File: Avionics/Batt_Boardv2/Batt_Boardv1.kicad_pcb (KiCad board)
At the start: 2 copper layers, 90.2 x 95.9 mm, 30 parts, among them J1 Conn_02x26_Odd_Even, J2 Conn_02x26_Odd_Even, Q1 IRF7458, Q2 IRF7458, U3 TMP36xS

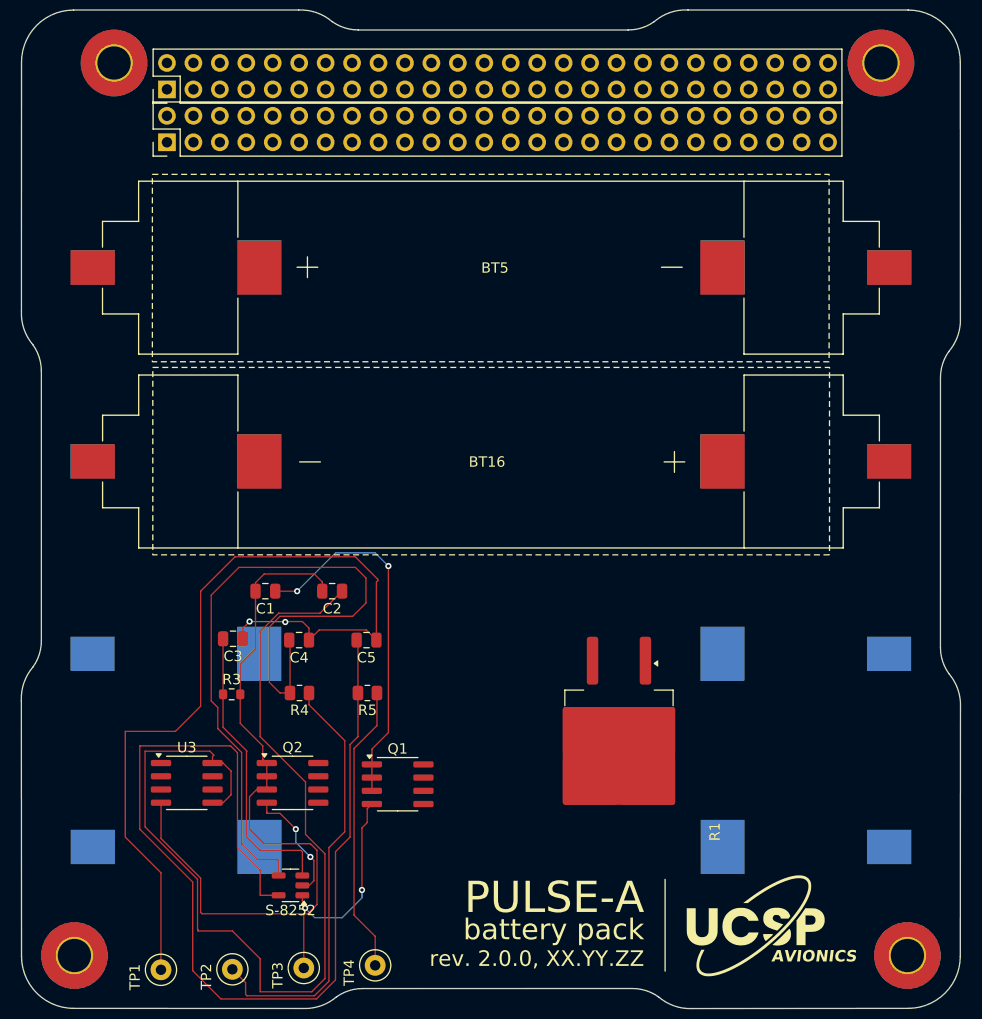
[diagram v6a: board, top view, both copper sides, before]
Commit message: 12/5/2024, Sephora Poteau: Finished the traces for all parts of the battery board.
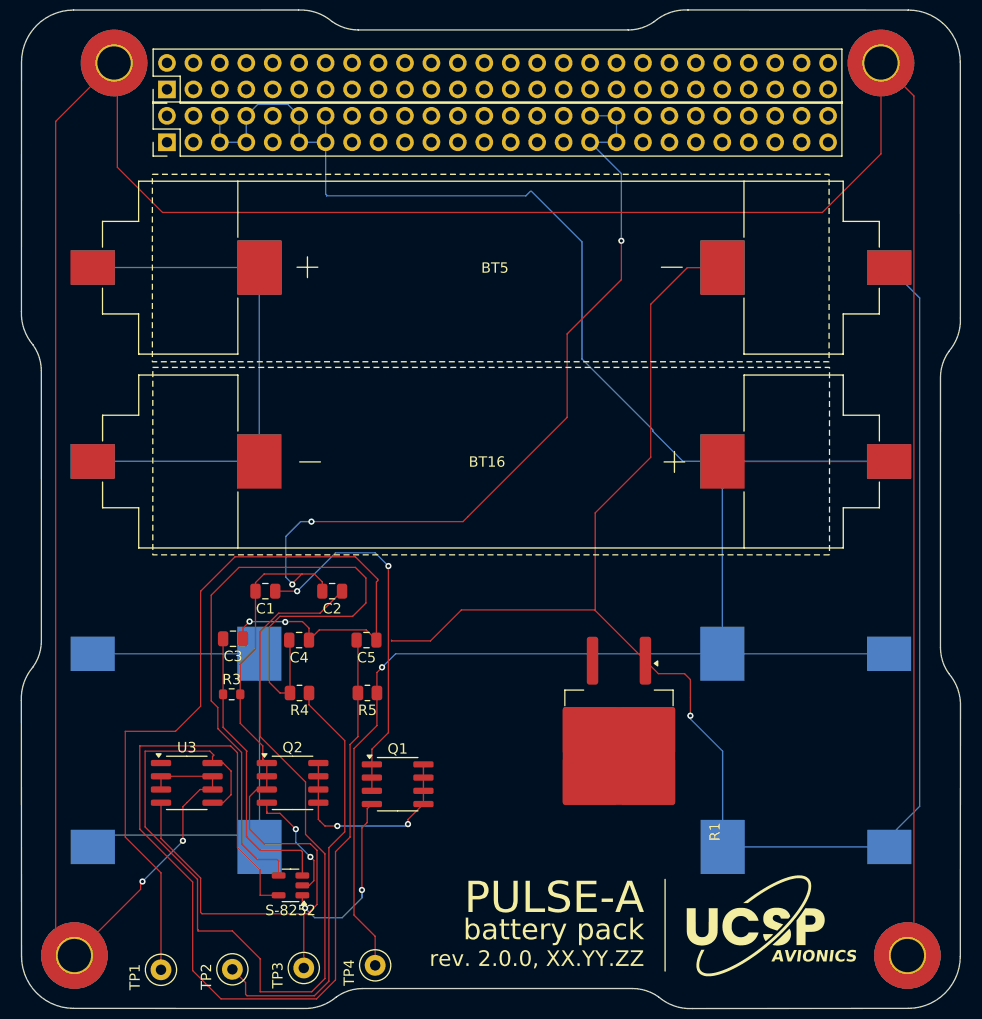
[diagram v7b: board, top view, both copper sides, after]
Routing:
- net (no net): track 0.00 -> 302.1 mm, vias 0 -> 2
- net /BATT_PRE_INH: track 27.9 -> 212.3 mm, vias 0 -> 1
- net /B-: track 85.3 -> 249.5 mm, vias 2 -> 3
- net GNDREF: track 76.0 -> 151.5 mm, vias 0 -> 3
- net Net-(BT1-BATT-): track 0.00 -> 51.5 mm
- net /BM: track 41.3 -> 92.0 mm
- net Net-(Q1-D-Pad5): track 0.00 -> 20.7 mm, vias 0 -> 2

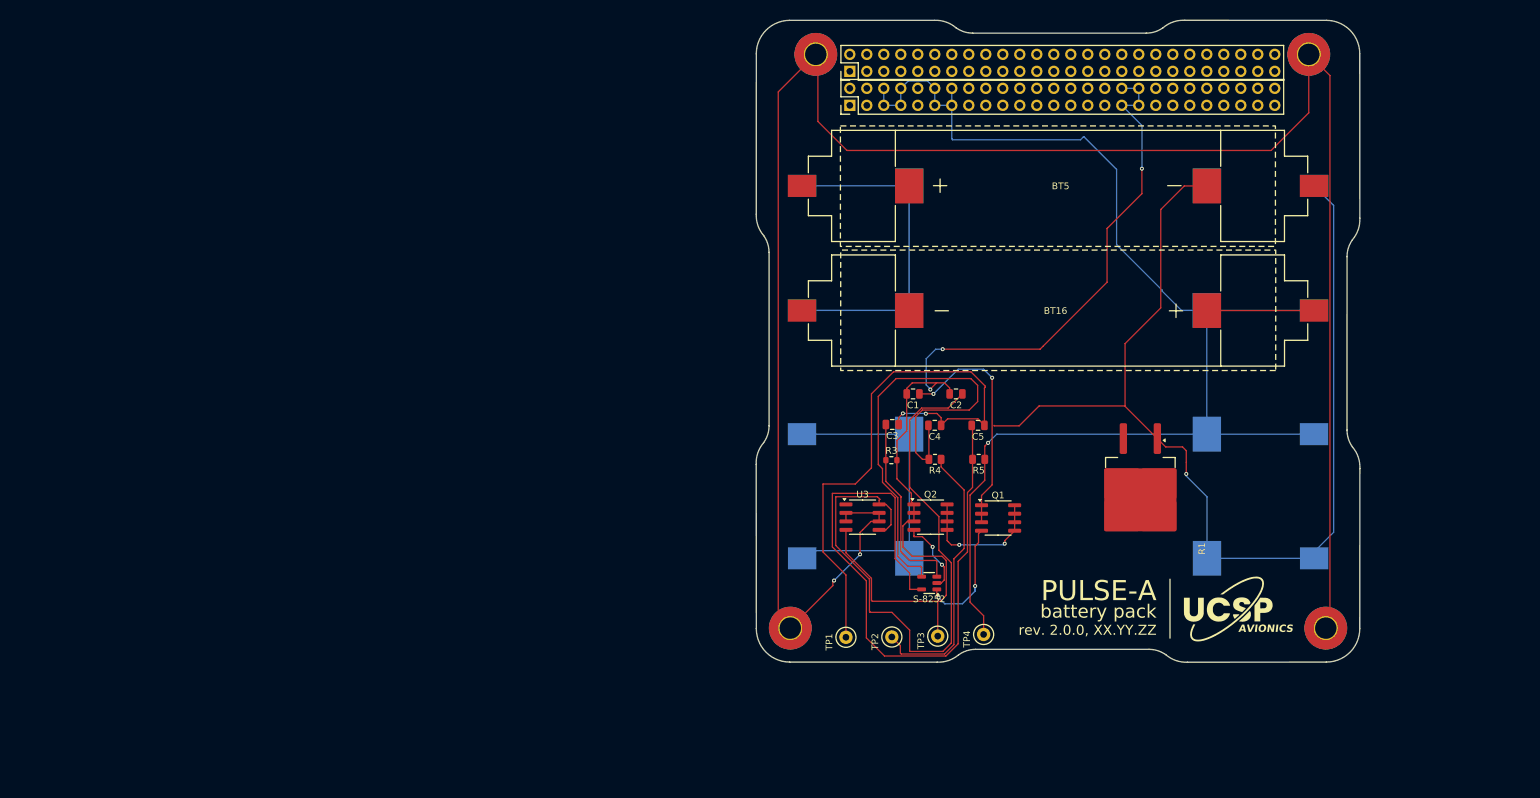
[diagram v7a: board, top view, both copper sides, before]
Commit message: 12/5/2024, Sephora Poteau: Finished adding traces, copper filled both front and back layers
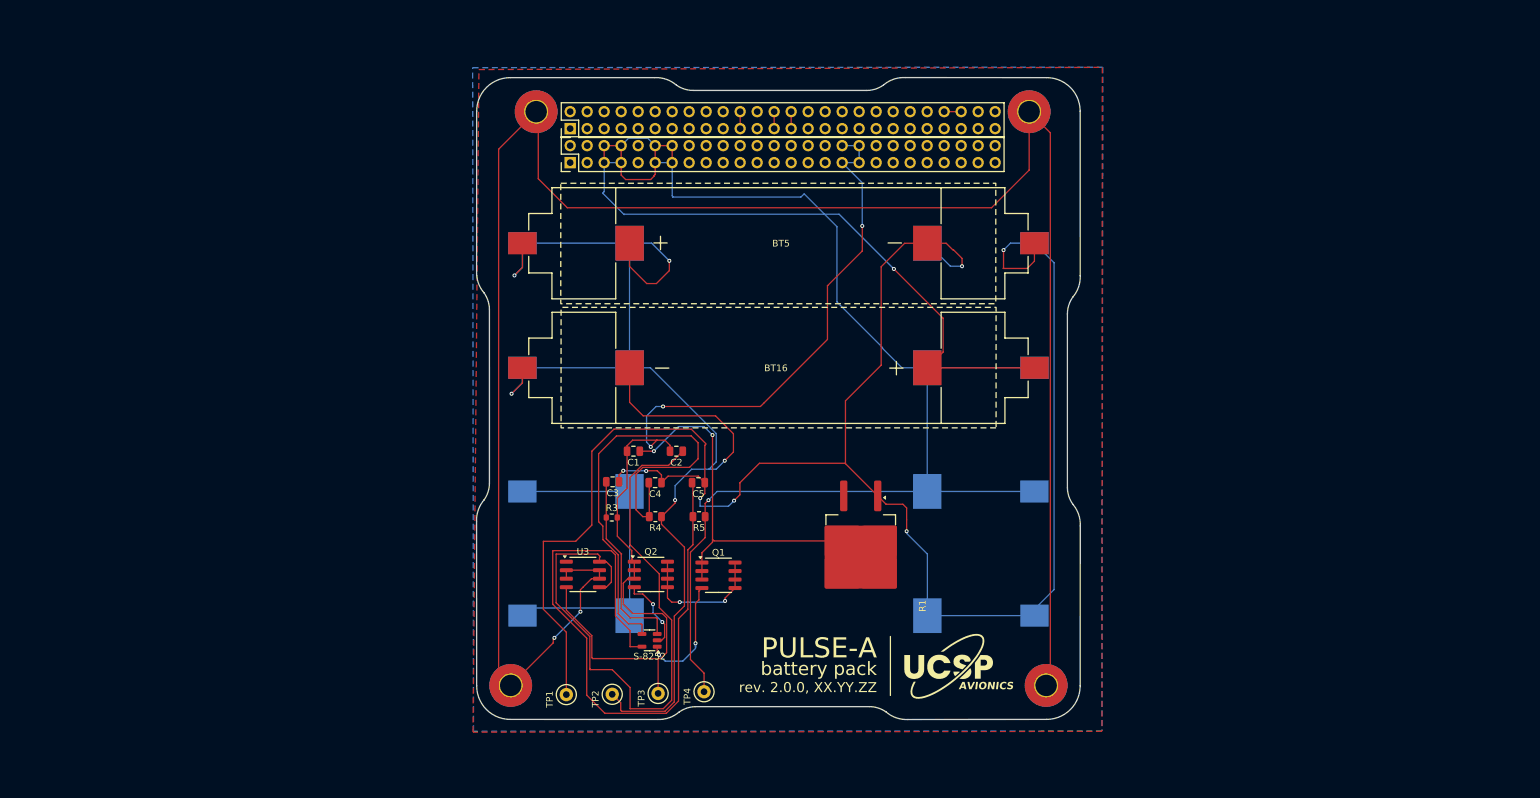
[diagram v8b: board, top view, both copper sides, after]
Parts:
- moved BT16 42.6 mm to (144.4, 93.0)
- moved G*** 42.6 mm to (170.0, 137.6)
- moved C1 42.6 mm to (123.1, 105.5)
- moved H1 42.6 mm to (108.5, 54.7)
- moved H4 42.6 mm to (104.7, 140.5)
- moved R3 42.6 mm to (119.8, 115.4)
- moved BT4 42.6 mm to (145.1, 130.1)
- moved BT1 42.6 mm to (144.3, 111.4)
- moved BT2 42.6 mm to (144.3, 93.0)
- moved BT3 42.6 mm to (145.1, 74.4)
- moved BT5 42.6 mm to (145.1, 74.4)
- moved C2 42.6 mm to (129.5, 105.5)
- moved C3 42.6 mm to (120.0, 110.0)
- moved C4 42.6 mm to (126.3, 110.2)
- moved C5 42.6 mm to (132.8, 110.2)
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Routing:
- net /BM: track 92.0 -> 195.8 mm, vias 0 -> 5
- net /BATT_PRE_INH: track 212.3 -> 298.4 mm, vias 1 -> 2
- net /B-: track 249.5 -> 287.4 mm, vias 3 -> 7
- net Net-(C1-Pad1): track 35.3 -> 70.0 mm
- net V_BATT: track 0.00 -> 2.54 mm
- net /EDFA_5V_SW: track 0.00 -> 2.54 mm
- net /5V_BUS: track 0.00 -> 2.54 mm
- net /3V3_BUS: track 0.00 -> 2.54 mm
- added copper zone on B.Cu, net GNDREF
- added copper zone on F.Cu, net GNDREF
